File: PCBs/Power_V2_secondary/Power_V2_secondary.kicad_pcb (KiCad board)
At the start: 2 copper layers, 40.1 x 84.3 mm, 14 parts, among them IC7 ACS712ELCTR-20A-T, J1 PCIE-164-02-F-D-TH-TR, J2 Conn_01x08, J8 Conn_01x02, U1 01530007Z

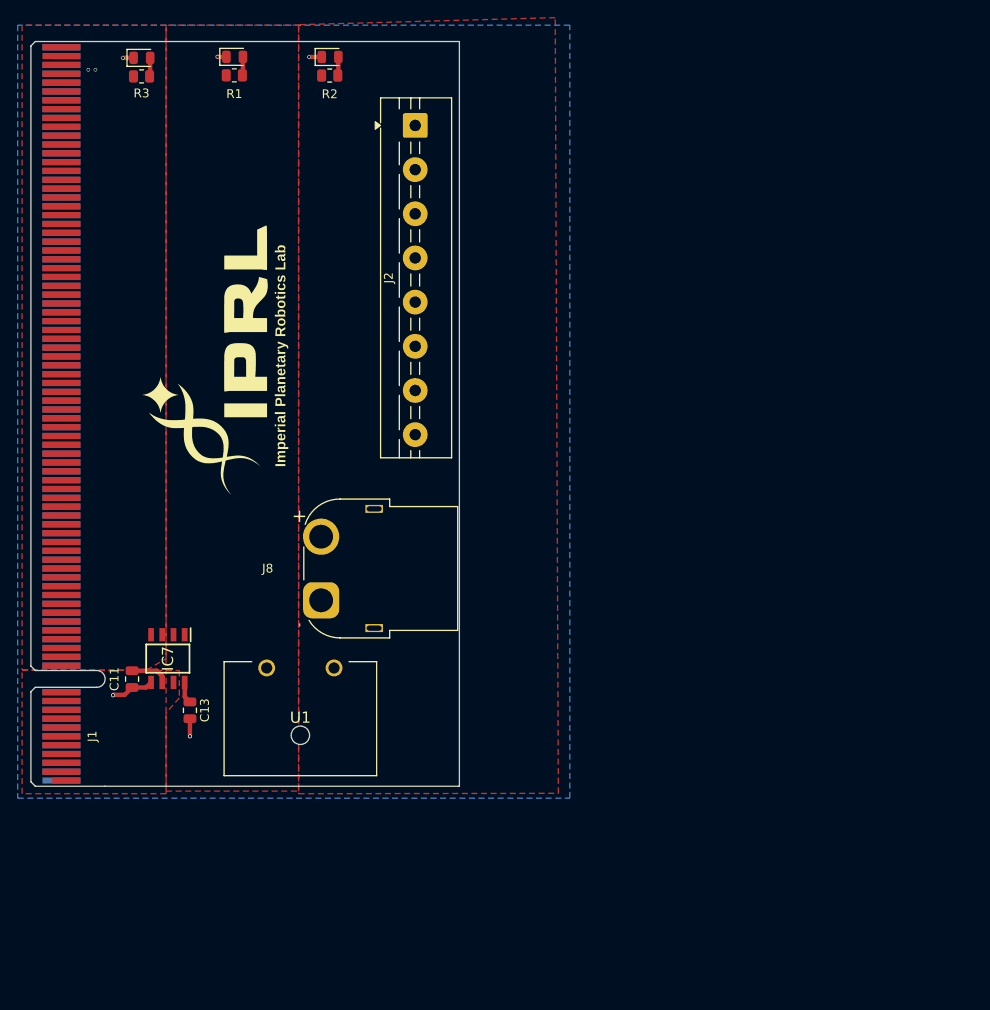
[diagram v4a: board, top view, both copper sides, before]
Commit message: stitching vias on secondary
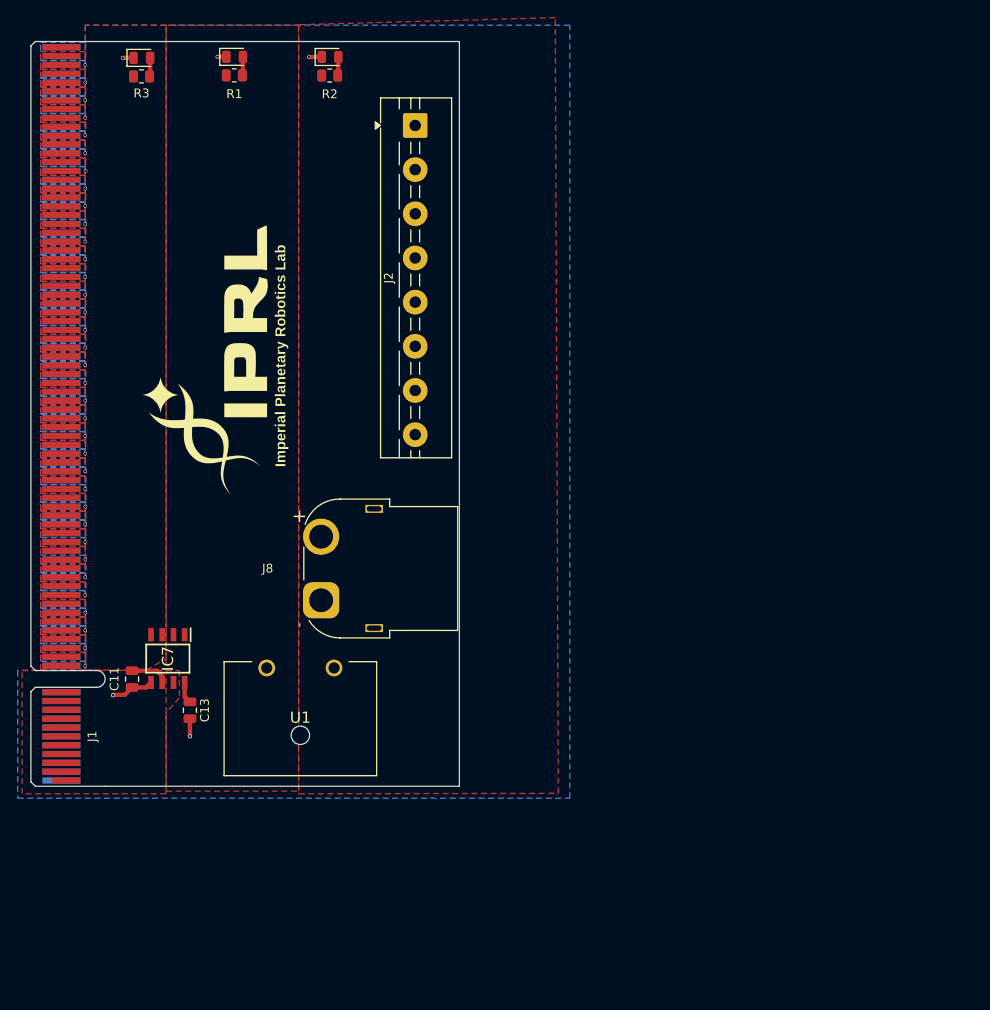
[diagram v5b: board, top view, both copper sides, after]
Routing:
- net GND: vias 5 -> 22
- net /14V8: vias 2 -> 18
- added copper zone on B.Cu, net /14V8
- added copper zone on F.Cu, net GND

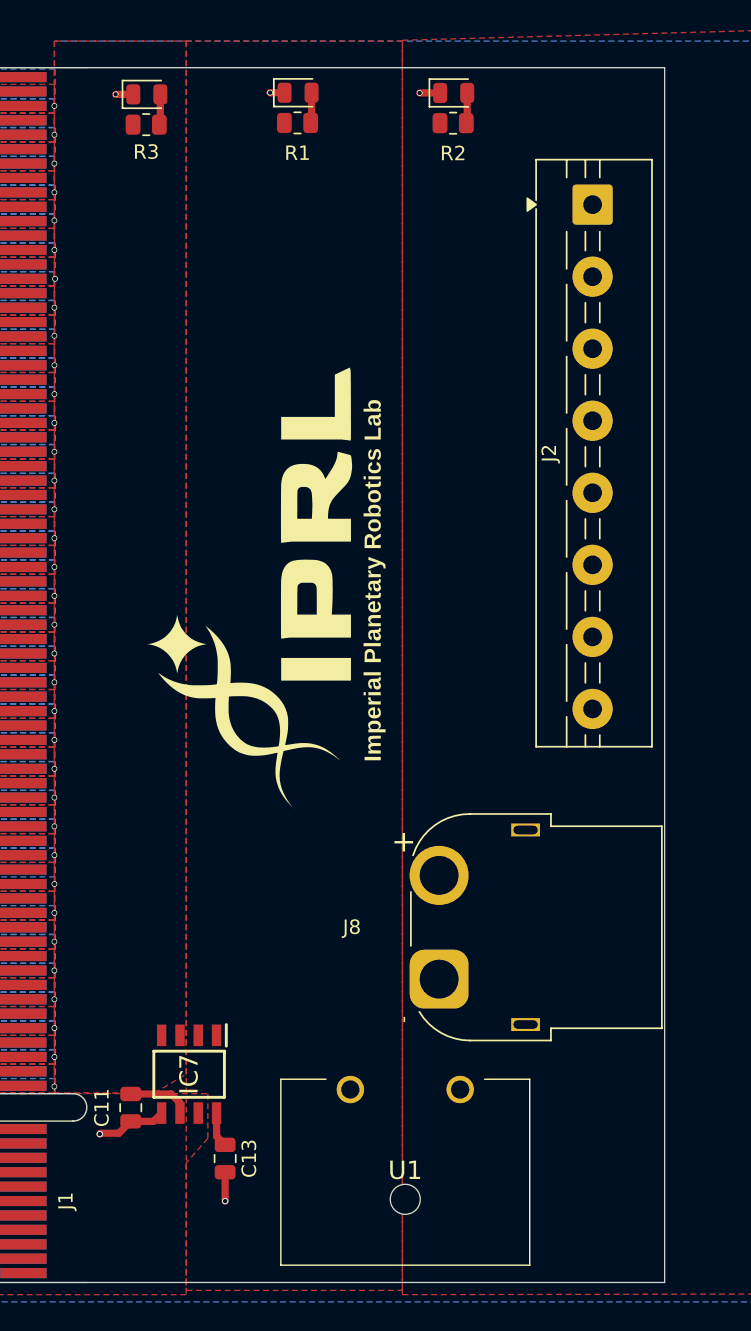
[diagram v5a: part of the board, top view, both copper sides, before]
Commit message: added mounting holes to secondary
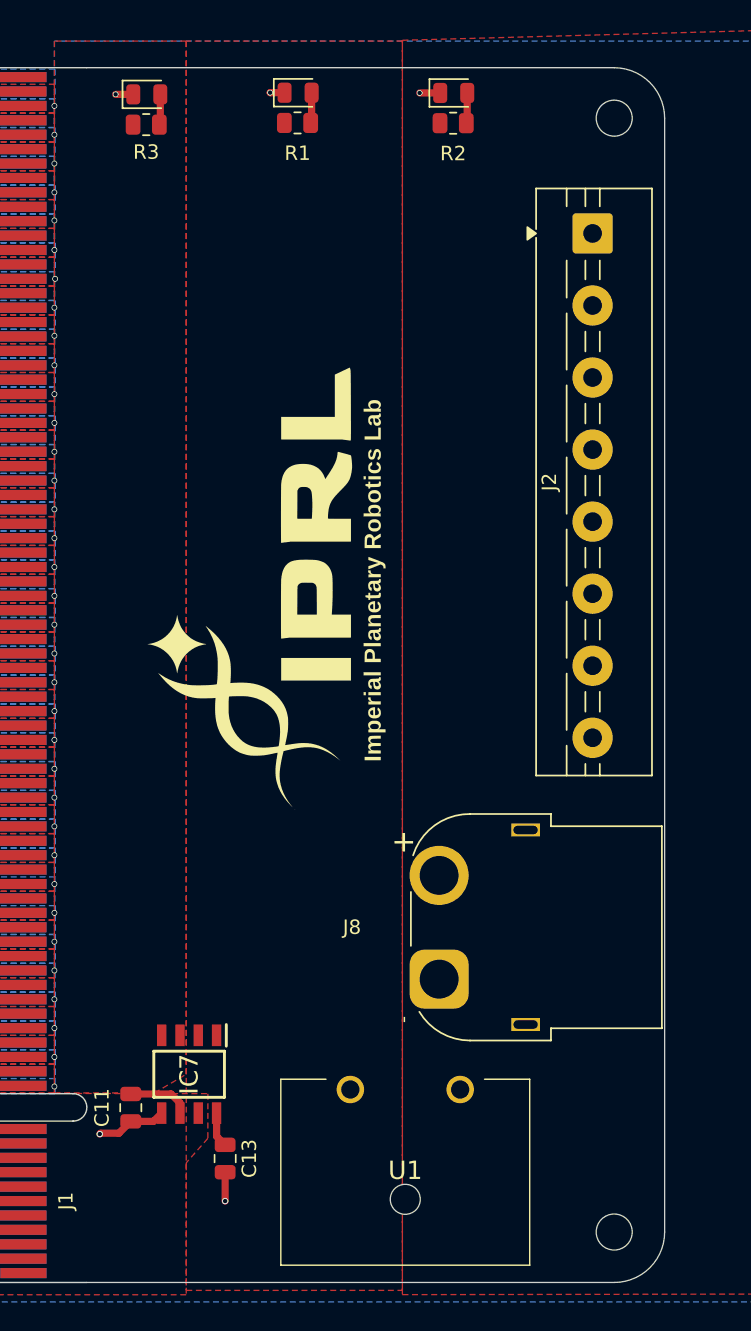
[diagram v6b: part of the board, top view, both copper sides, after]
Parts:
- added H1: MountingHole, MountingHole:MountingHole_2.5mm, F.Cu at (86.5, 100.2)
- added H2: MountingHole, MountingHole:MountingHole_2.5mm, F.Cu at (86.5, 22.9)
- moved J2 2.00 mm to (85.0, 30.9)
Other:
- outline, holes or cut-outs redrawn
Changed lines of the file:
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@@
 		)
 	)
+	(footprint "MountingHole:MountingHole_2.5mm"
+		(layer "F.Cu")
+		(at 86.5 22.85)
+		(descr "Mounting Hole 2.5mm, no annular, generated by kicad-footprint-generator mountinghole.py")
+		(tags "mountinghole")
+		(property "Reference" "H2"
+			(at 0 -3.45 0)
+			(layer "F.SilkS")
+			(hide yes)
+			(effects
+				(font
+					(size 1 1)
+					(thickness 0.15)
+				)
+			)
+		)
+		(property "Value" "MountingHole"
+			(at 0 3.45 0)
+			(layer "F.Fab")
+			(effects
+				(font
+					(size 1 1)
+					(thickness 0.15)
+				)
+			)
+		)
+		(property "Datasheet" ""
+			(at 0 0 0)
+			(layer "F.Fab")
+			(hide yes)
+			(effects
+				(font
+					(size 1.27 1.27)
+					(thickness 0.15)
+				)
+			)
+		)
+		(property "Description" "Mounting Hole without connection"
+			(at 0 0 0)
+			(layer "F.Fab")
+			(hide yes)
+			(effects
+				(font
+					(size 1.27 1.27)
+					(thickness 0.15)
+				)
+			)
+		)
+		(property ki_fp_filters "MountingHole*")
+		(sheetname "/")
+		(sheetfile "Power_V2_secondary.kicad_sch")
+		(attr exclude_from_pos_files exclude_from_bom)
+		(fp_circle
+			(center 0 0)
+			(end 2.5 0)
+			(stroke
+				(width 0.15)
+				(type solid)
+			)
+			(fill no)
+			(layer "Cmts.User")
+		)
+		(fp_circle
+			(center 0 0)
+			(end 2.75 0)
+			(stroke
+				(width 0.05)
+				(type solid)
+			)
+			(fill no)
+			(layer "F.CrtYd")
+		)
+		(fp_text user "${REFERENCE}"
+			(at 0 0 0)
+			(layer "F.Fab")
+			(effects
+				(font
+					(size 1 1)
+					(thickness 0.15)
+				)
+			)
+		)
+		(pad "" np_thru_hole circle
+			(at 0 0)
+			(size 2.5 2.5)
+			(drill 2.5)
+			(layers "*.Cu" "*.Mask")
+		)
+		(embedded_fonts no)
+	)
 	(footprint "main_lib:IPRL_31mm"
 		(layer "F.Cu")
@@
 	(footprint "TerminalBlock:TerminalBlock_MaiXu_MX126-5.0-08P_1x08_P5.00mm"
 		(layer "F.Cu")
-		(at 85 28.85 -90)
+		(at 85 30.85 -90)
 		(descr "terminal block MaiXu MX126-5.0-08P, 8 pins, pitch 5mm, size 40.5x7.8mm, drill diameter 1.3mm, pad diameter 2.8mm, https://www.lcsc.com/datasheet/lcsc_datasheet_2309150913_MAX-MX126-5-0-03P-GN01-Cu-S-A_C5188435.pdf, script-generated using https://gitlab.com/kicad/libraries/kicad-footprint-generator/-/tree/master/scripts/TerminalBlock_MaiXu")
 		(tags "THT terminal block MaiXu MX126-5.0-08P pitch 5mm size 40.5x7.8mm drill 1.3mm pad 2.8mm")
@@
 		)
 	)
+	(footprint "MountingHole:MountingHole_2.5mm"
+		(layer "F.Cu")
+		(at 86.5 100.15)
+		(descr "Mounting Hole 2.5mm, no annular, generated by kicad-footprint-generator mountinghole.py")
+		(tags "mountinghole")
+		(property "Reference" "H1"
+			(at 0 -3.45 0)
+			(layer "F.SilkS")
+			(hide yes)
+			(effects
+				(font
+					(size 1 1)
+					(thickness 0.15)
+				)
+			)
+		)
+		(property "Value" "MountingHole"
+			(at 0 3.45 0)
+			(layer "F.Fab")
+			(effects
+				(font
+					(size 1 1)
+					(thickness 0.15)
+				)
+			)
+		)
+		(property "Datasheet" ""
+			(at 0 0 0)
+			(layer "F.Fab")
+			(hide yes)
+			(effects
+				(font
+					(size 1.27 1.27)
+					(thickness 0.15)
+				)
+			)
+		)
+		(property "Description" "Mounting Hole without connection"
+			(at 0 0 0)
+			(layer "F.Fab")
+			(hide yes)
+			(effects
+				(font
+					(size 1.27 1.27)
+					(thickness 0.15)
+				)
+			)
+		)
+		(property ki_fp_filters "MountingHole*")
+		(sheetname "/")
+		(sheetfile "Power_V2_secondary.kicad_sch")
+		(attr exclude_from_pos_files exclude_from_bom)
+		(fp_circle
+			(center 0 0)
+			(end 2.5 0)
+			(stroke
+				(width 0.15)
+				(type solid)
+			)
+			(fill no)
+			(layer "Cmts.User")
+		)
+		(fp_circle
+			(center 0 0)
+			(end 2.75 0)
+			(stroke
+				(width 0.05)
+				(type solid)
+			)
+			(fill no)
+			(layer "F.CrtYd")
+		)
+		(fp_text user "${REFERENCE}"
+			(at 0 0 0)
+			(layer "F.Fab")
+			(effects
+				(font
+					(size 1 1)
+					(thickness 0.15)
+				)
+			)
+		)
+		(pad "" np_thru_hole circle
+			(at 0 0)
+			(size 2.5 2.5)
+			(drill 2.5)
+			(layers "*.Cu" "*.Mask")
+		)
+		(embedded_fonts no)
+	)
 	(footprint "Connector_PCBEdge:BUS_PCIexpress_x16"
 		(layer "B.Cu")
@@
 	(gr_line
 		(start 49.9 103.65)
-		(end 90 103.65)
+		(end 86.5 103.65)
 		(stroke
 			(width 0.05)
@@
 		(layer "Edge.Cuts")
 	)
+	(gr_arc
+		(start 90 100.15)
+		(mid 88.974874 102.624874)
+		(end 86.5 103.65)
+		(stroke
+			(width 0.05)
+			(type default)
+		)
+		(layer "Edge.Cuts")
+	)
 	(gr_line
-		(start 90 103.65)
-		(end 90 19.35)
+		(start 90 100.15)
+		(end 90 22.85)
+		(stroke
+			(width 0.05)
+			(type default)
+		)
+		(layer "Edge.Cuts")
+	)
+	(gr_arc
+		(start 86.5 19.35)
+		(mid 88.974874 20.375126)
+		(end 90 22.85)
 		(stroke
 			(width 0.05)
@@
 	(gr_line
 		(start 49.9 19.35)
-		(end 90 19.35)
+		(end 86.5 19.35)
 		(stroke
 			(width 0.05)

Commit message: Changes from meeting
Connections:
- J1 pad B1: Net-(J1-PadB1) -> GND
- J1 pad B10: Net-(J1-PadB1) -> GND
- J1 pad B11: Net-(J1-PadB1) -> GND
- J1 pad B2: Net-(J1-PadB1) -> GND
- J1 pad B3: Net-(J1-PadB1) -> GND
- J1 pad B4: Net-(J1-PadB1) -> GND
- J1 pad B5: Net-(J1-PadB1) -> GND
- J1 pad B6: Net-(J1-PadB1) -> GND
- J1 pad B7: Net-(J1-PadB1) -> GND
- J1 pad B8: Net-(J1-PadB1) -> GND
- J1 pad B9: Net-(J1-PadB1) -> GND
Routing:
- net /14V8_OUT: track 0.00 -> 61.8 mm
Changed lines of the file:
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@@
 			(psa4output no)
 			(plot_black_and_white yes)
+			(plotinvisibletext no)
 			(sketchpadsonfab no)
 			(plotpadnumbers no)
@@
 	(net 9 "Net-(D2-A)")
 	(net 10 "Net-(D3-A)")
-	(net 11 "Net-(J1-PadB1)")
 	(footprint "iprl_footprints:01530007Z"
 		(layer "F.Cu")
@@
 			(size 0.7 4.3)
 			(layers "B.Cu" "B.Mask")
-			(net 11 "Net-(J1-PadB1)")
+			(net 2 "GND")
 			(pinfunction "B1")
 			(pintype "passive")
@@
 			(size 0.7 4.3)
 			(layers "B.Cu" "B.Mask")
-			(net 11 "Net-(J1-PadB1)")
+			(net 2 "GND")
 			(pinfunction "B2")
 			(pintype "passive")
@@
 			(size 0.7 4.3)
 			(layers "B.Cu" "B.Mask")
-			(net 11 "Net-(J1-PadB1)")
+			(net 2 "GND")
 			(pinfunction "B3")
 			(pintype "passive")
@@
 			(size 0.7 4.3)
 			(layers "B.Cu" "B.Mask")
-			(net 11 "Net-(J1-PadB1)")
+			(net 2 "GND")
 			(pinfunction "B4")
 			(pintype "passive")
@@
 			(size 0.7 4.3)
 			(layers "B.Cu" "B.Mask")
-			(net 11 "Net-(J1-PadB1)")
+			(net 2 "GND")
 			(pinfunction "B5")
 			(pintype "passive")
@@
 			(size 0.7 4.3)
 			(layers "B.Cu" "B.Mask")
-			(net 11 "Net-(J1-PadB1)")
+			(net 2 "GND")
 			(pinfunction "B6")
 			(pintype "passive")
@@
 			(size 0.7 4.3)
 			(layers "B.Cu" "B.Mask")
-			(net 11 "Net-(J1-PadB1)")
+			(net 2 "GND")
 			(pinfunction "B7")
 			(pintype "passive")
@@
 			(size 0.7 4.3)
 			(layers "B.Cu" "B.Mask")
-			(net 11 "Net-(J1-PadB1)")
+			(net 2 "GND")
 			(pinfunction "B8")
 			(pintype "passive")
@@
 			(size 0.7 4.3)
 			(layers "B.Cu" "B.Mask")
-			(net 11 "Net-(J1-PadB1)")
+			(net 2 "GND")
 			(pinfunction "B9")
 			(pintype "passive")
@@
 			(size 0.7 4.3)
 			(layers "B.Cu" "B.Mask")
-			(net 11 "Net-(J1-PadB1)")
+			(net 2 "GND")
 			(pinfunction "B10")
 			(pintype "passive")
@@
 			(size 0.7 4.3)
 			(layers "B.Cu" "B.Mask")
-			(net 11 "Net-(J1-PadB1)")
+			(net 2 "GND")
 			(pinfunction "B11")
 			(pintype "passive")
@@
 	)
 	(segment
+		(start 65.4 84.05)
+		(end 65.3 84.15)
+		(width 0.2)
+		(layer "F.Cu")
+		(net 5)
+	)
+	(segment
+		(start 63.61 23.46)
+		(end 65.4 25.25)
+		(width 0.2)
+		(layer "F.Cu")
+		(net 5)
+	)
+	(segment
+		(start 63.61 23.18)
+		(end 63.61 23.46)
+		(width 0.2)
+		(layer "F.Cu")
+		(net 5)
+	)
+	(segment
+		(start 65.4 25.25)
+		(end 65.4 84.05)
+		(width 0.2)
+		(layer "F.Cu")
+		(net 5)
+	)
+	(segment
 		(start 65.5 21.085)
 		(end 65.5 23.115)
@@
 		(polygon
 			(pts
-				(xy 71.8 104.496815) (xy 101.2 104.45) (xy 100.85 16.65) (xy 71.8 17.44525)
+				(xy 66.000396 104.50605) (xy 101.2 104.45) (xy 100.85 16.65) (xy 66.000396 17.604015)
 			)
 		)
@@
 		(layer "F.Cu")
 		(hatch edge 0.5)
-		(priority 3)
 		(connect_pads yes
 			(clearance 0.5)
@@
 		(polygon
 			(pts
-				(xy 47.65 90.5) (xy 54.586957 90.5) (xy 56.8 89.2) (xy 56.8 17.5) (xy 47.65 17.5)
+				(xy 47.65 90.5) (xy 54.586957 90.5) (xy 64.7 84.559331) (xy 64.7 17.5) (xy 47.65 17.5)
 			)
 		)
@@
 		(polygon
 			(pts
-				(xy 56.8 104.2) (xy 71.8 104.2) (xy 71.8 17.5) (xy 56.8 17.5)
+				(xy 56.8 104.2) (xy 71.8 104.2) (xy 71.8 82.4) (xy 56.8 82.4)
 			)
 		)
@@
 		(hatch edge 0.5)
 		(priority 2)
-		(connect_pads
+		(connect_pads yes
 			(clearance 0.5)
 		)

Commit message: follow up changes from meeting
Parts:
- H1, H2: footprint MountingHole:MountingHole_2.5mm -> MountingHole:MountingHole_2.7mm_M2.5_DIN965_Pad_TopBottom
- J2: value Conn_01x08 -> Conn_01x10; footprint TerminalBlock:TerminalBlock_MaiXu_MX126-5.0-08P_1x08_P5.00mm -> TerminalBlock:TerminalBlock_MaiXu_MX126-5.0-10P_1x10_P5.00mm
- moved J8 50.6 mm to (120.0, 104.5)
- moved C11 50.6 mm to (98.5, 113.5)
- moved C13 50.6 mm to (105.1, 117.0)
- moved H1 50.6 mm to (132.1, 122.1)
- moved IC7 50.6 mm to (102.6, 111.2)
- moved J1 50.6 mm to (90.5, 125.0)
- moved U1 50.6 mm to (117.6, 118.0)
- moved R1 48.4 mm to (111.3, 35.4)
- moved R3 48.4 mm to (100.8, 35.5)
- moved D1 48.4 mm to (111.4, 33.3)
- moved D2 48.4 mm to (122.2, 33.3)
- moved D3 48.4 mm to (100.9, 33.4)
- moved R2 48.4 mm to (122.1, 35.4)
- moved G*** 47.9 mm to (108.2, 69.7)
- moved J2 47.3 mm to (130.6, 43.3)
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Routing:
- net /14V8_OUT: track 61.8 -> 71.0 mm
- net /14V8: track 0.00 -> 2.78 mm
- net GND: vias 22 -> 23
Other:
- board size 40.1 x 84.3 mm -> 44.9 x 99.8 mm
- board text added: "14V8"
- board text added: "GND"
